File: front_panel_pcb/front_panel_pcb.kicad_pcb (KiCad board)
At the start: 2 copper layers, 93.3 x 100 mm, 41 parts

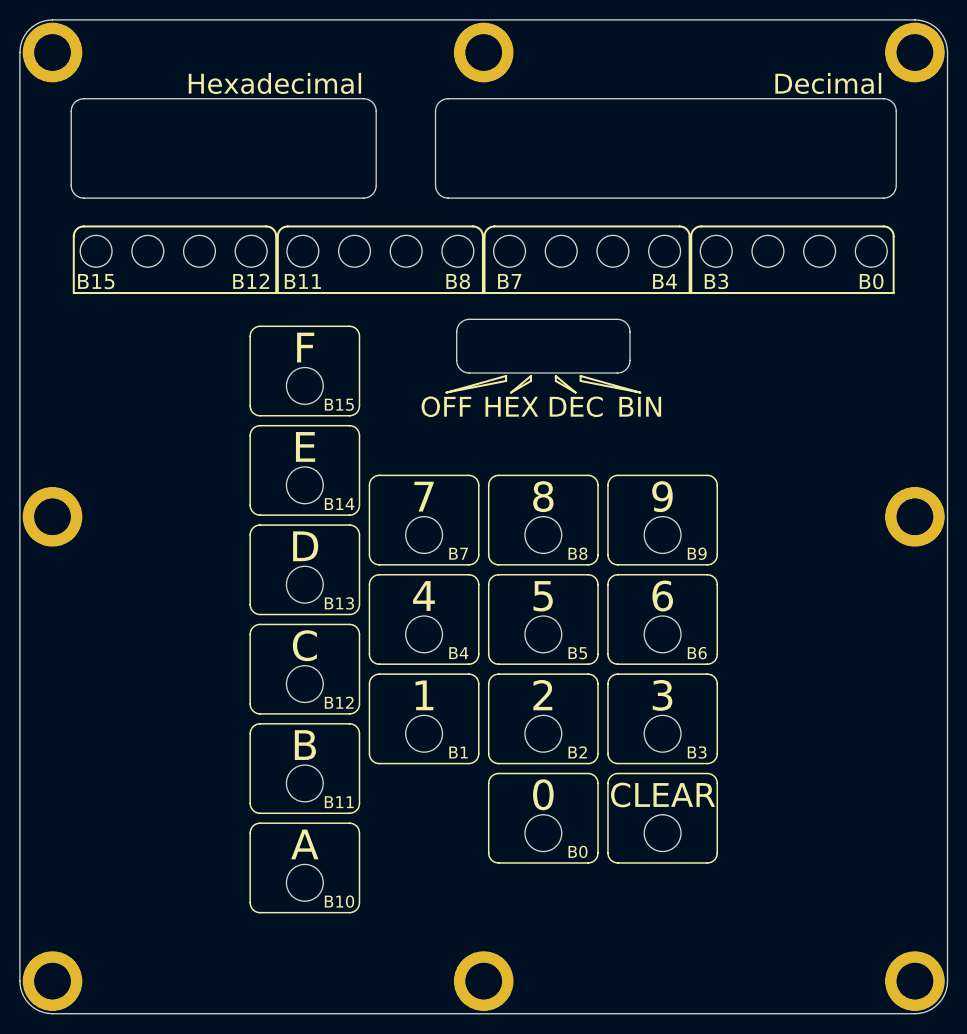
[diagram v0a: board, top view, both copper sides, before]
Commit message: change pcb standoff holes for 2.5mm hex
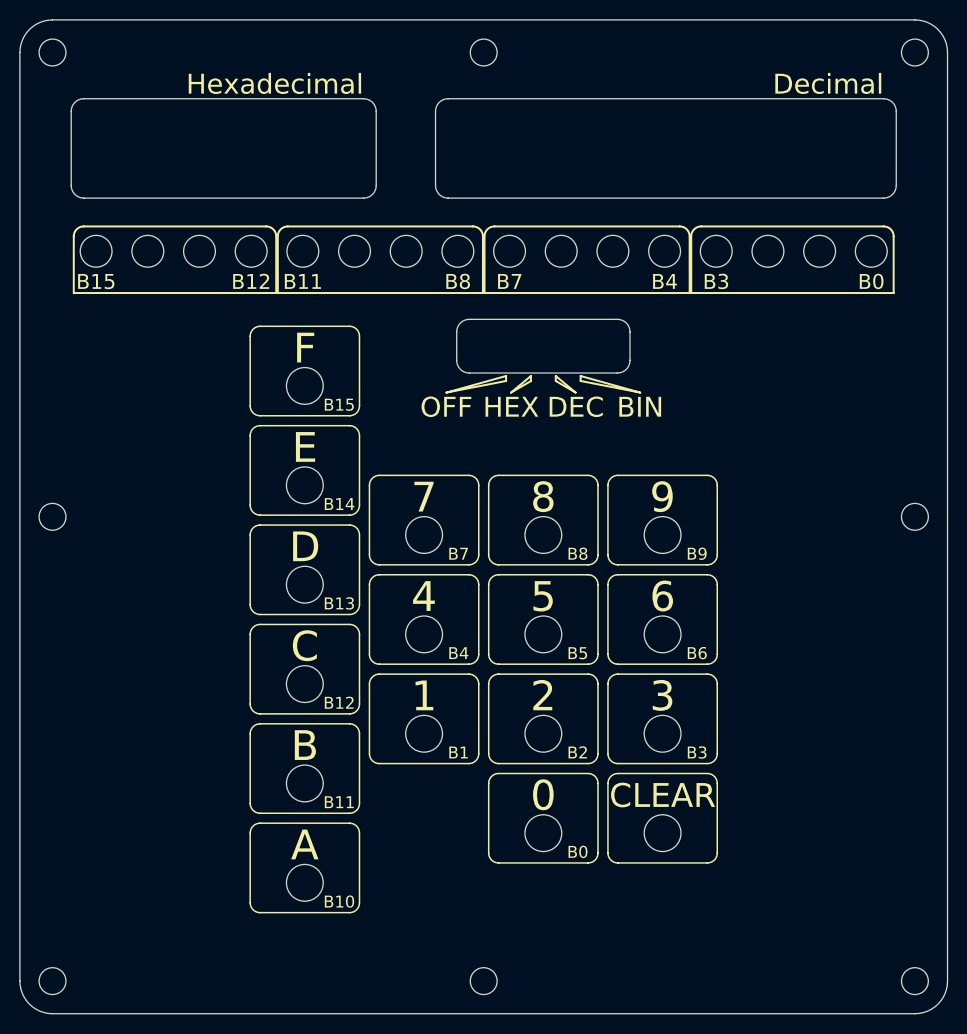
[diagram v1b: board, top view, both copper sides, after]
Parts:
- removed the REF** at (56.6, 53.3)
- removed the REF** at (100.0, 53.3)
- removed the REF** at (143.4, 53.3)
- removed the REF** at (143.4, 100.0)
- removed the REF** at (143.4, 146.7)
- removed the REF** at (100.0, 146.7)
- removed the REF** at (56.6, 146.7)
- removed the REF** at (56.6, 100.0)
- added REF**: MountingHole_2.7mm_M2.5, Mounting_Holes:MountingHole_2.7mm_M2.5, F.Cu at (143.4, 146.7)
- added REF**: MountingHole_2.7mm_M2.5, Mounting_Holes:MountingHole_2.7mm_M2.5, F.Cu at (100.0, 146.7)
- added REF**: MountingHole_2.7mm_M2.5, Mounting_Holes:MountingHole_2.7mm_M2.5, F.Cu at (56.6, 146.7)
- added REF**: MountingHole_2.7mm_M2.5, Mounting_Holes:MountingHole_2.7mm_M2.5, F.Cu at (143.4, 100.0)
- added REF**: MountingHole_2.7mm_M2.5, Mounting_Holes:MountingHole_2.7mm_M2.5, F.Cu at (56.6, 53.3)
- added REF**: MountingHole_2.7mm_M2.5, Mounting_Holes:MountingHole_2.7mm_M2.5, F.Cu at (56.6, 100.0)
- added REF**: MountingHole_2.7mm_M2.5, Mounting_Holes:MountingHole_2.7mm_M2.5, F.Cu at (143.4, 53.3)
- added REF**: MountingHole_2.7mm_M2.5, Mounting_Holes:MountingHole_2.7mm_M2.5, F.Cu at (100.0, 53.3)
